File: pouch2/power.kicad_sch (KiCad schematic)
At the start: 20 parts, among them J10 Conn_01x02_Male, J11 Conn_01x02_Male, J12 Conn_01x02_Male, J9 Conn_01x02_Male, Q1 AO3401A, Q2 AO3401A, Q3 AO3401A, Q4 AO3401A, SW1 SW_SPDT

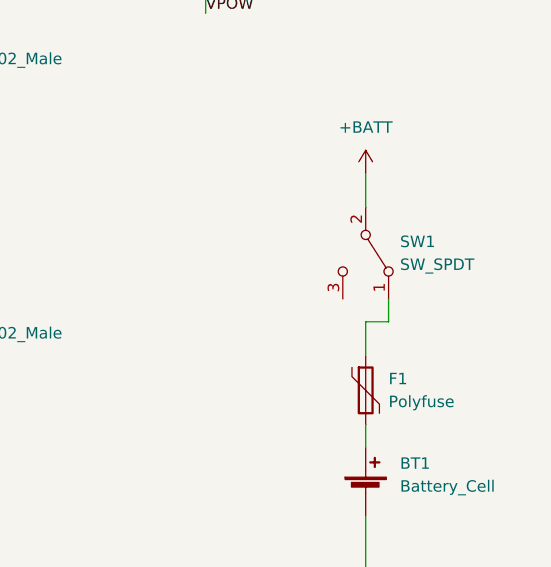
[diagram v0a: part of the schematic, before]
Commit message: added pi zero header
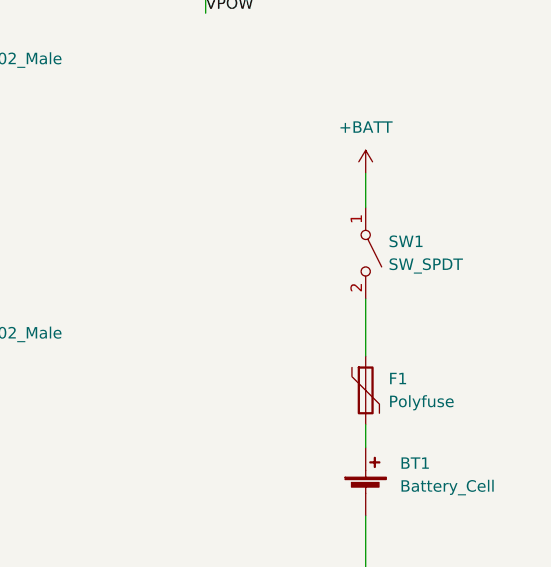
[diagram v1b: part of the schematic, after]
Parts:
- F1: footprint (none) -> Fuse:Fuse_BelFuse_0ZRE0005FF_L8.3mm_W3.8mm
- J10, J11, J12, J9: footprint (none) -> Connector_PinHeader_2.54mm:PinHeader_1x02_P2.54mm_Horizontal
- R33, R34, R35, R44, R45, R46, R47, R48, R49: footprint (none) -> Resistor_SMD:R_0815_2038Metric
- SW1: footprint (none) -> Connector_PinHeader_2.54mm:PinHeader_1x02_P2.54mm_Horizontal; symbol Switch:SW_SPDT -> Switch:SW_SPST
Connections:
- net +BATT: now also SW1.1 (A); no longer SW1.2 (B)
- net at F1.1: now also SW1.2 (B); no longer SW1.1 (A)
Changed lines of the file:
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@@
 	(wire
 		(pts
-			(xy 127 71.12) (xy 127 74.93)
+			(xy 127 68.58) (xy 127 74.93)
 		)
 		(stroke
@@
 	(wire
 		(pts
-			(xy 129.54 68.58) (xy 129.54 71.12)
-		)
-		(stroke
-			(width 0)
-			(type default)
-		)
-	)
-	(wire
-		(pts
 			(xy 46.99 128.27) (xy 55.88 128.27)
 		)
@@
 		(pts
 			(xy 46.99 45.72) (xy 48.26 45.72)
-		)
-		(stroke
-			(width 0)
-			(type default)
-		)
-	)
-	(wire
-		(pts
-			(xy 129.54 71.12) (xy 127 71.12)
 		)
 		(stroke
@@
 			)
 		)
-		(property "Footprint" ""
+		(property "Footprint" "Resistor_SMD:R_0815_2038Metric"
 			(at 41.91 138.938 90)
 			(effects
@@
 			)
 		)
-		(property "Footprint" ""
+		(property "Footprint" "Connector_PinHeader_2.54mm:PinHeader_1x02_P2.54mm_Horizontal"
 			(at 76.2 72.39 0)
 			(effects
@@
 			)
 		)
-		(property "Footprint" ""
+		(property "Footprint" "Fuse:Fuse_BelFuse_0ZRE0005FF_L8.3mm_W3.8mm"
 			(at 128.27 83.82 0)
 			(effects
@@
 			)
 		)
-		(property "Footprint" ""
+		(property "Footprint" "Resistor_SMD:R_0815_2038Metric"
 			(at 41.91 77.978 90)
 			(effects
@@
 			)
 		)
-		(property "Footprint" ""
+		(property "Footprint" "Resistor_SMD:R_0815_2038Metric"
 			(at 107.442 27.94 90)
 			(effects
@@
 			)
 		)
-		(property "Footprint" ""
+		(property "Footprint" "Connector_PinHeader_2.54mm:PinHeader_1x02_P2.54mm_Horizontal"
 			(at 76.2 102.87 0)
 			(effects
@@
 			)
 		)
-		(property "Footprint" ""
+		(property "Footprint" "Resistor_SMD:R_0815_2038Metric"
 			(at 41.91 108.458 90)
 			(effects
@@
 			)
 		)
-		(property "Footprint" ""
+		(property "Footprint" "Resistor_SMD:R_0815_2038Metric"
 			(at 48.768 101.6 90)
 			(effects
@@
 			)
 		)
-		(property "Footprint" ""
+		(property "Footprint" "Resistor_SMD:R_0815_2038Metric"
 			(at 48.768 40.64 90)
 			(effects
@@
 			)
 		)
-		(property "Footprint" ""
+		(property "Footprint" "Resistor_SMD:R_0815_2038Metric"
 			(at 41.91 47.498 90)
 			(effects
@@
 			)
 		)
-		(property "Footprint" ""
+		(property "Footprint" "Connector_PinHeader_2.54mm:PinHeader_1x02_P2.54mm_Horizontal"
 			(at 76.2 41.91 0)
 			(effects
@@
 			)
 		)
-		(property "Footprint" ""
+		(property "Footprint" "Resistor_SMD:R_0815_2038Metric"
 			(at 48.768 71.12 90)
 			(effects
@@
 			)
 		)
-		(property "Footprint" ""
+		(property "Footprint" "Resistor_SMD:R_0815_2038Metric"
 			(at 48.768 132.08 90)
 			(effects
@@
 	)
 	(symbol
-		(lib_id "Switch:SW_SPDT")
+		(lib_id "Switch:SW_SPST")
 		(at 127 63.5 270)
 		(unit 1)
@@
 		(fields_autoplaced yes)
 		(property "Reference" "SW1"
-			(at 130.81 62.2299 90)
+			(at 129.54 62.2299 90)
 			(effects
 				(font
@@
 		)
 		(property "Value" "SW_SPDT"
-			(at 130.81 64.7699 90)
-			(effects
-				(font
-					(size 1.27 1.27)
-				)
-				(justify left)
-			)
-		)
-		(property "Footprint" ""
+			(at 129.54 64.7699 90)
+			(effects
+				(font
+					(size 1.27 1.27)
+				)
+				(justify left)
+			)
+		)
+		(property "Footprint" "Connector_PinHeader_2.54mm:PinHeader_1x02_P2.54mm_Horizontal"
 			(at 127 63.5 0)
 			(effects
@@
 			)
 		)
-		(property "Description" "Switch, single pole double throw"
+		(property "Description" "Single Pole Single Throw (SPST) switch"
 			(at 127 63.5 0)
 			(effects
@@
 		)
 		(pin "1"
-		)
-		(pin "3"
 		)
 		(pin "2"
@@
 			)
 		)
-		(property "Footprint" ""
+		(property "Footprint" "Connector_PinHeader_2.54mm:PinHeader_1x02_P2.54mm_Horizontal"
 			(at 76.2 133.35 0)
 			(effects

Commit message: started PCB design
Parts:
- BT501: renamed from BT1; footprint (none) -> Battery:BatteryHolder_Keystone_1042_1x18650
- J501: renamed from J9; footprint Connector_PinHeader_2.54mm:PinHeader_1x02_P2.54mm_Horizontal -> Connector_PinHeader_2.54mm:PinHeader_1x02_P2.54mm_Vertical
- J502: renamed from J10; footprint Connector_PinHeader_2.54mm:PinHeader_1x02_P2.54mm_Horizontal -> Connector_PinHeader_2.54mm:PinHeader_1x02_P2.54mm_Vertical
- J503: renamed from J11; footprint Connector_PinHeader_2.54mm:PinHeader_1x02_P2.54mm_Horizontal -> Connector_PinHeader_2.54mm:PinHeader_1x02_P2.54mm_Vertical
- J504: renamed from J12; footprint Connector_PinHeader_2.54mm:PinHeader_1x02_P2.54mm_Horizontal -> Connector_PinHeader_2.54mm:PinHeader_1x02_P2.54mm_Vertical
- R501: renamed from R33; footprint Resistor_SMD:R_0815_2038Metric -> Resistor_SMD:R_0805_2012Metric
- R502: renamed from R35; footprint Resistor_SMD:R_0815_2038Metric -> Resistor_SMD:R_0805_2012Metric
- R503: renamed from R45; footprint Resistor_SMD:R_0815_2038Metric -> Resistor_SMD:R_0805_2012Metric
- R504: renamed from R46; footprint Resistor_SMD:R_0815_2038Metric -> Resistor_SMD:R_0805_2012Metric
- R505: renamed from R34; footprint Resistor_SMD:R_0815_2038Metric -> Resistor_SMD:R_0805_2012Metric
- R506: renamed from R44; footprint Resistor_SMD:R_0815_2038Metric -> Resistor_SMD:R_0805_2012Metric
- R507: renamed from R47; footprint Resistor_SMD:R_0815_2038Metric -> Resistor_SMD:R_0805_2012Metric
- R508: renamed from R48; footprint Resistor_SMD:R_0815_2038Metric -> Resistor_SMD:R_0805_2012Metric
- R509: renamed from R49; footprint Resistor_SMD:R_0815_2038Metric -> Resistor_SMD:R_0805_2012Metric
- SW501: renamed from SW1; footprint Connector_PinHeader_2.54mm:PinHeader_1x02_P2.54mm_Horizontal -> Connector_PinHeader_2.54mm:PinHeader_1x02_P2.54mm_Vertical
- renumbered F1 to F501, Q1 to Q501, Q2 to Q502, Q3 to Q503, Q4 to Q504

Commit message: PCB and footprint arrangements
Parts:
- BT501: footprint Battery:BatteryHolder_Keystone_1042_1x18650 -> SensorBoards:18650_Keystone_1043
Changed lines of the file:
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@@
 			)
 		)
-		(property "Footprint" "Battery:BatteryHolder_Keystone_1042_1x18650"
+		(property "Footprint" "SensorBoards:18650_Keystone_1043"
 			(at 127 88.646 90)
 			(effects

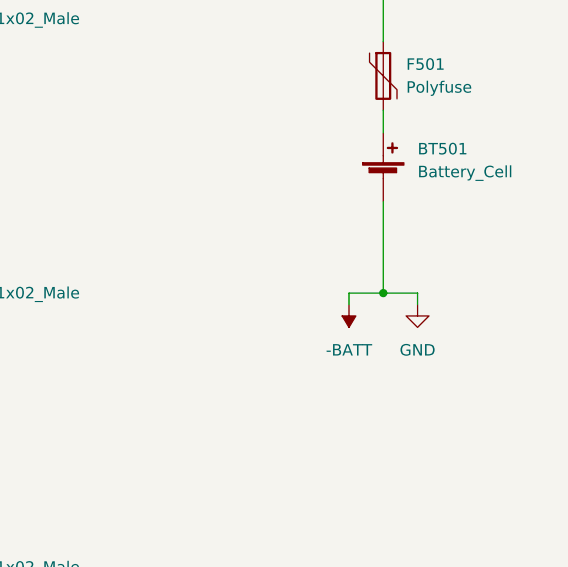
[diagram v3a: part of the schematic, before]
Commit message: updated backside of PCB
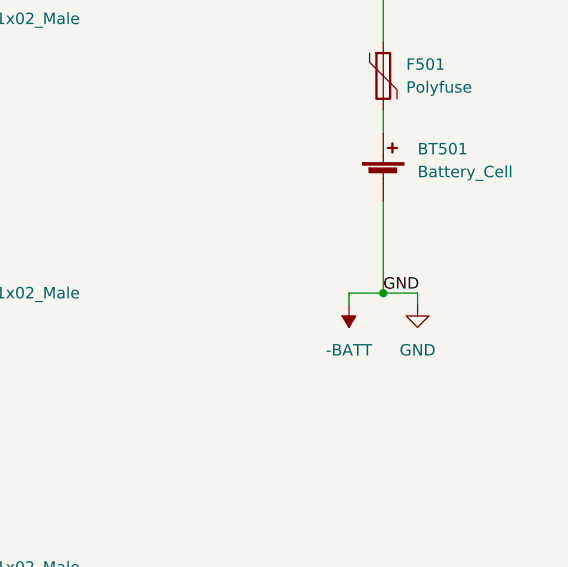
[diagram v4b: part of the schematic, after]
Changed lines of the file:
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@@
+		)
+	)
+	(label "GND"
+		(at 127 102.87 0)
+		(fields_autoplaced yes)
+		(effects
+			(font
+				(size 1.27 1.27)
+			)
+			(justify left bottom)
 		)
 	)

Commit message: minor updates
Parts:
- R509: value R -> 0
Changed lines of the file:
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@@
 			)
 		)
-		(property "Value" "R"
+		(property "Value" "0"
 			(at 111.76 29.2099 0)
 			(effects

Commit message: started routing
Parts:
- added JP501, JP502: Jumper_2_Open, Jumper:SolderJumper-2_P1.3mm_Open_TrianglePad1.0x1.5mm, symbol Jumper:Jumper_2_Open
- added JP503: Jumper_2_Bridged, Jumper:SolderJumper-2_P1.3mm_Bridged2Bar_Pad1.0x1.5mm, symbol Jumper:SolderJumper_2_Bridged
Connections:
- net +BATT: now also JP502.1 (A)
- net at F501.1, SW501.2 (B): now also JP501.1 (A)
- net -BATT: no longer names the net of BT501.2 (-)
- net -BATT: now also JP503.2 (B)
- new net GND: JP503.1 (A)
- new net HMI_S43: JP502.2 (B)
- new net HMI_S44: JP501.2 (B)
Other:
- note added: "HMI_S43/S44 can be used as an additional Power On-Switch."
- note added: "TODO: Charging/Undervoltage Circuitry"
- moved on the sheet: BT501, F501, SW501

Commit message: drawed a lot of things
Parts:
- added R510, R511, R512, R513, R514, R515, R516, R517, R518, R519, R520, R521, R522, R523, R524, R525, R526, R527, R528, R529, R530, R531, R532, R533, R534, R535, R536, R537, R538, R539, R540, R541: 0, Resistor_SMD:R_0805_2012Metric, symbol Device:R
- renumbered JP503 to JP501, JP501 to JP503
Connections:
- net VCC_S1: now also R510.2, R511.2, R512.2, R513.2; no longer J501.1 (Pin_1), Q501.2 (S)
- net VCC_S2: now also R526.2, R530.2, R534.2, R538.2; no longer J502.1 (Pin_1), Q502.2 (S)
- net VCC_S3: now also R514.2, R515.2, R516.2, R517.2; no longer J503.1 (Pin_1), Q503.2 (S)
- net VCC_S4: now also R527.2, R531.2, R535.2, R539.2; no longer J504.1 (Pin_1), Q504.2 (S)
- new net VCC_CON1: J501.1 (Pin_1), Q501.2 (S), R512.1, R514.1, R518.1, R522.1, R526.1, R527.1, R528.1, R529.1
- new net VCC_CON2: J502.1 (Pin_1), Q502.2 (S), R513.1, R515.1, R519.1, R523.1, R530.1, R531.1, R532.1, R533.1
- new net VCC_CON3: J503.1 (Pin_1), Q503.2 (S), R511.1, R516.1, R520.1, R524.1, R534.1, R535.1, R536.1, R537.1
- new net VCC_CON4: J504.1 (Pin_1), Q504.2 (S), R510.1, R517.1, R521.1, R525.1, R538.1, R539.1, R540.1, R541.1
- new net VCC_S5: R518.2, R519.2, R520.2, R521.2
- new net VCC_S6: R528.2, R532.2, R536.2, R540.2
- new net VCC_S7: R522.2, R523.2, R524.2, R525.2
- new net VCC_S8: R529.2, R533.2, R537.2, R541.2

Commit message: finished first routing pass
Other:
- moved on the sheet: R509
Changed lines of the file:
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@@
 	(wire
 		(pts
-			(xy 109.22 31.75) (xy 109.22 36.83)
+			(xy 114.3 36.83) (xy 114.3 41.91)
 		)
 		(stroke
@@
 	(wire
 		(pts
-			(xy 109.22 21.59) (xy 109.22 24.13)
+			(xy 114.3 24.13) (xy 114.3 29.21)
 		)
 		(stroke
@@
 	)
 	(label "VPOW"
-		(at 109.22 36.83 0)
+		(at 114.3 41.91 0)
 		(fields_autoplaced yes)
 		(effects
@@
 		(length 2.54)
 		(shape round)
+		(at 114.3 27.94 90)
+		(fields_autoplaced yes)
+		(effects
+			(font
+				(size 1.27 1.27)
+			)
+			(justify left bottom)
+		)
+		(property "Netclass" "Thick"
+			(at 111.76 27.2415 90)
+			(effects
+				(font
+					(size 1.27 1.27)
+					(italic yes)
+				)
+				(justify left)
+			)
+		)
+	)
+	(netclass_flag ""
+		(length 2.54)
+		(shape round)
 		(at 240.03 26.67 0)
 		(fields_autoplaced yes)
@@
 		(length 2.54)
 		(shape round)
-		(at 109.22 33.02 90)
+		(at 114.3 38.1 90)
 		(fields_autoplaced yes)
 		(effects
@@
 		)
 		(property "Netclass" "Thick"
-			(at 106.68 32.3215 90)
+			(at 111.76 37.4015 90)
 			(effects
 				(font
@@
 	(symbol
 		(lib_id "Device:R")
-		(at 109.22 27.94 0)
+		(at 114.3 33.02 0)
 		(unit 1)
 		(exclude_from_sim no)
@@
 		(fields_autoplaced yes)
 		(property "Reference" "R509"
-			(at 111.76 26.6699 0)
+			(at 116.84 31.7499 0)
 			(effects
 				(font
@@
 		)
 		(property "Value" "0"
-			(at 111.76 29.2099 0)
+			(at 116.84 34.2899 0)
 			(effects
 				(font
@@
 		)
 		(property "Footprint" "Resistor_SMD:R_0805_2012Metric"
-			(at 107.442 27.94 90)
+			(at 112.522 33.02 90)
 			(effects
 				(font
@@
 		)
 		(property "Datasheet" "~"
-			(at 109.22 27.94 0)
+			(at 114.3 33.02 0)
 			(effects
 				(font
@@
 		)
 		(property "Description" "Resistor"
-			(at 109.22 27.94 0)
+			(at 114.3 33.02 0)
 			(effects
 				(font
@@
 	(symbol
 		(lib_id "power:+3.3V")
-		(at 109.22 21.59 0)
+		(at 114.3 24.13 0)
 		(unit 1)
 		(exclude_from_sim no)
@@
 		(fields_autoplaced yes)
 		(property "Reference" "#PWR0501"
-			(at 109.22 25.4 0)
+			(at 114.3 27.94 0)
 			(effects
 				(font
@@
 		)
 		(property "Value" "+3.3V"
-			(at 109.22 16.51 0)
+			(at 114.3 19.05 0)
 			(effects
 				(font
@@
 		)
 		(property "Footprint" ""
-			(at 109.22 21.59 0)
+			(at 114.3 24.13 0)
 			(effects
 				(font
@@
 		)
 		(property "Datasheet" ""
-			(at 109.22 21.59 0)
+			(at 114.3 24.13 0)
 			(effects
 				(font
@@
 		)
 		(property "Description" "Power symbol creates a global label with name \"+3.3V\""
-			(at 109.22 21.59 0)
+			(at 114.3 24.13 0)
 			(effects
 				(font
